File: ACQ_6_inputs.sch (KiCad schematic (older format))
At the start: 0 parts

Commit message: Layout done for ADC + LVDS and DAC -> FPGA
Signed-off-by: Alexis Jeandet <alexis.jeandet@member.fsf.org>
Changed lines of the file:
@@
 $EndDescr
 $Sheet
-S 3275 800  1450 1350
+S 3250 2550 1450 1350
 U 5F3E1AE5
 F0 "Sheet5F3E1AE4" 50
 F1 "ADC_circuit.sch" 50
-F2 "IN+" I L 3275 1225 50
-F3 "IN-" I L 3275 1350 50
+F2 "IN+" I L 3250 2975 50
+F3 "IN-" I L 3250 3100 50
+F4 "V+" I R 4700 2700 50
+F5 "V-" I R 4700 2600 50
+F6 "VDDL" I R 4700 2900 50
+F7 "OVDD" I R 4700 3000 50
+F8 "CNV" I R 4700 3350 50
+F9 "CLK" I R 4700 3450 50
+F10 "DA" I R 4700 3650 50
+F11 "DCO" I R 4700 3550 50
+F12 "VDD" I R 4700 2800 50
 $EndSheet
 Text HLabel 2975 1225 0    50   Input ~ 0
@@
 Wire Wire Line
 	2975 1350 3275 1350
-$Sheet
-S 3250 2550 1450 1350
-U 5F766F53
-F0 "sheet5F766F53" 50
-F1 "ADC_circuit.sch" 50
-F2 "IN+" I L 3250 2975 50
-F3 "IN-" I L 3250 3100 50
-$EndSheet
 Text HLabel 2950 2975 0    50   Input ~ 0
 CH2_IN+
@@
 	2950 3100 3250 3100
 $Sheet
-S 3250 4250 1450 1350
+S 6600 950  1450 1350
 U 5F7670FC
 F0 "sheet5F7670FC" 50
 F1 "ADC_circuit.sch" 50
-F2 "IN+" I L 3250 4675 50
-F3 "IN-" I L 3250 4800 50
+F2 "IN+" I L 6600 1375 50
+F3 "IN-" I L 6600 1500 50
+F4 "V+" I R 8050 1050 50
+F5 "V-" I R 8050 1175 50
+F6 "VDDL" I R 8050 1300 50
+F7 "OVDD" I R 8050 1425 50
+F8 "CNV" I R 8050 1850 50
+F9 "CLK" I R 8050 1950 50
+F10 "DA" I R 8050 2150 50
+F11 "DCO" I R 8050 2050 50
+F12 "VDD" I R 8050 1550 50
 $EndSheet
 Text HLabel 2950 4675 0    50   Input ~ 0
@@
 Wire Wire Line
 	2950 4800 3250 4800
-$Sheet
-S 6600 950  1450 1350
-U 5F7672A2
-F0 "sheet5F7672A2" 50
-F1 "ADC_circuit.sch" 50
-F2 "IN+" I L 6600 1375 50
-F3 "IN-" I L 6600 1500 50
-$EndSheet
 Text HLabel 6300 1375 0    50   Input ~ 0
 CH4_IN+
@@
 F2 "IN+" I L 6600 2975 50
 F3 "IN-" I L 6600 3100 50
+F4 "V+" I R 8050 2675 50
+F5 "V-" I R 8050 2750 50
+F6 "VDDL" I R 8050 2850 50
+F7 "OVDD" I R 8050 2925 50
+F8 "CNV" I R 8050 3475 50
+F9 "CLK" I R 8050 3575 50
+F10 "DA" I R 8050 3775 50
+F11 "DCO" I R 8050 3675 50
+F12 "VDD" I R 8050 3050 50
 $EndSheet
 Text HLabel 6300 2975 0    50   Input ~ 0
@@
 Wire Wire Line
 	6300 3100 6600 3100
-$Sheet
-S 6575 4200 1450 1350
+Text HLabel 6275 4600 0    50   Input ~ 0
+CH6_IN+
+Text HLabel 6275 4725 0    50   Input ~ 0
+CH6_IN-
+Wire Wire Line
+	6275 4600 6575 4600
+Wire Wire Line
+	6275 4725 6575 4725
+$Sheet
+S 6575 4175 1450 1350
+U 5F766F53
+F0 "sheet5F766F53" 50
+F1 "ADC_circuit.sch" 50
+F2 "IN+" I L 6575 4600 50
+F3 "IN-" I L 6575 4725 50
+F4 "V+" I R 8025 4250 50
+F5 "V-" I R 8025 4350 50
+F6 "VDDL" I R 8025 4550 50
+F7 "OVDD" I R 8025 4650 50
+F8 "CNV" I R 8025 5025 50
+F9 "CLK" I R 8025 5125 50
+F10 "DA" I R 8025 5325 50
+F11 "DCO" I R 8025 5225 50
+F12 "VDD" I R 8025 4450 50
+$EndSheet
+$Sheet
+S 3250 4250 1450 1350
 U 5F76778E
 F0 "sheet5F76778E" 50
 F1 "ADC_circuit.sch" 50
-F2 "IN+" I L 6575 4625 50
-F3 "IN-" I L 6575 4750 50
-$EndSheet
-Text HLabel 6275 4625 0    50   Input ~ 0
-CH6_IN+
-Text HLabel 6275 4750 0    50   Input ~ 0
-CH6_IN-
-Wire Wire Line
-	6275 4625 6575 4625
-Wire Wire Line
-	6275 4750 6575 4750
+F2 "IN+" I L 3250 4675 50
+F3 "IN-" I L 3250 4800 50
+F4 "V+" I R 4700 4325 50
+F5 "V-" I R 4700 4425 50
+F6 "VDDL" I R 4700 4525 50
+F7 "OVDD" I R 4700 4625 50
+F8 "CNV" I R 4700 5125 50
+F9 "CLK" I R 4700 5225 50
+F10 "DA" I R 4700 5425 50
+F11 "DCO" I R 4700 5325 50
+F12 "VDD" I R 4700 4725 50
+$EndSheet
+Text HLabel 4925 1700 2    50   Input ~ 0
+ADC1_CNV
+Text HLabel 4925 1800 2    50   Input ~ 0
+ADC1_CLK
+Text HLabel 4925 1900 2    50   Input ~ 0
+ADC1_DCO
+Text HLabel 4925 2000 2    50   Input ~ 0
+ADC1_DA
+Wire Wire Line
+	4725 1700 4925 1700
+Wire Wire Line
+	4725 1800 4925 1800
+Wire Wire Line
+	4725 1900 4925 1900
+Wire Wire Line
+	4725 2000 4925 2000
+Text HLabel 8250 1850 2    50   Input ~ 0
+ADC4_CNV
+Text HLabel 8250 1950 2    50   Input ~ 0
+ADC4_CLK
+Text HLabel 8250 2050 2    50   Input ~ 0
+ADC4_DCO
+Text HLabel 8250 2150 2    50   Input ~ 0
+ADC4_DA
+Wire Wire Line
+	8050 1850 8250 1850
+Wire Wire Line
+	8050 1950 8250 1950
+Wire Wire Line
+	8050 2050 8250 2050
+Wire Wire Line
+	8050 2150 8250 2150
+Text HLabel 8250 3475 2    50   Input ~ 0
+ADC5_CNV
+Text HLabel 8250 3575 2    50   Input ~ 0
+ADC5_CLK
+Text HLabel 8250 3675 2    50   Input ~ 0
+ADC5_DCO
+Text HLabel 8250 3775 2    50   Input ~ 0
+ADC5_DA
+Wire Wire Line
+	8050 3475 8250 3475
+Wire Wire Line
+	8050 3575 8250 3575
+Wire Wire Line
+	8050 3675 8250 3675
+Wire Wire Line
+	8050 3775 8250 3775
+Text HLabel 8225 5025 2    50   Input ~ 0
+ADC6_CNV
+Text HLabel 8225 5125 2    50   Input ~ 0
+ADC6_CLK
+Text HLabel 8225 5225 2    50   Input ~ 0
+ADC6_DCO
+Text HLabel 8225 5325 2    50   Input ~ 0
+ADC6_DA
+Wire Wire Line
+	8025 5025 8225 5025
+Wire Wire Line
+	8025 5125 8225 5125
+Wire Wire Line
+	8025 5225 8225 5225
+Wire Wire Line
+	8025 5325 8225 5325
+Text HLabel 4900 5125 2    50   Input ~ 0
+ADC3_CNV
+Text HLabel 4900 5225 2    50   Input ~ 0
+ADC3_CLK
+Text HLabel 4900 5325 2    50   Input ~ 0
+ADC3_DCO
+Text HLabel 4900 5425 2    50   Input ~ 0
+ADC3_DA
+Wire Wire Line
+	4700 5125 4900 5125
+Wire Wire Line
+	4700 5225 4900 5225
+Wire Wire Line
+	4700 5325 4900 5325
+Wire Wire Line
+	4700 5425 4900 5425
+Text HLabel 4900 3350 2    50   Input ~ 0
+ADC2_CNV
+Text HLabel 4900 3450 2    50   Input ~ 0
+ADC2_CLK
+Text HLabel 4900 3550 2    50   Input ~ 0
+ADC2_DCO
+Text HLabel 4900 3650 2    50   Input ~ 0
+ADC2_DA
+Wire Wire Line
+	4700 3350 4900 3350
+Wire Wire Line
+	4700 3450 4900 3450
+Wire Wire Line
+	4700 3550 4900 3550
+Wire Wire Line
+	4700 3650 4900 3650
+$Sheet
+S 3275 800  1450 1350
+U 5F7672A2
+F0 "sheet5F7672A2" 50
+F1 "ADC_circuit.sch" 50
+F2 "IN+" I L 3275 1225 50
+F3 "IN-" I L 3275 1350 50
+F4 "V+" I R 4725 875 50
+F5 "V-" I R 4725 975 50
+F6 "VDDL" I R 4725 1100 50
+F7 "OVDD" I R 4725 1200 50
+F8 "CNV" I R 4725 1700 50
+F9 "CLK" I R 4725 1800 50
+F10 "DA" I R 4725 2000 50
+F11 "DCO" I R 4725 1900 50
+F12 "VDD" I R 4725 1325 50
+$EndSheet
 $EndSCHEMATC

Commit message: Layout complete, needs silk screen cleanup and few checks
Signed-off-by: Alexis Jeandet <alexis.jeandet@member.fsf.org>
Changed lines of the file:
@@
 F2 "IN+" I L 3250 2975 50
 F3 "IN-" I L 3250 3100 50
-F4 "V+" I R 4700 2700 50
-F5 "V-" I R 4700 2600 50
+F4 "V+" I R 4700 2600 50
+F5 "V-" I R 4700 2700 50
 F6 "VDDL" I R 4700 2900 50
 F7 "OVDD" I R 4700 3000 50
@@
 F5 "V-" I R 4700 4425 50
 F6 "VDDL" I R 4700 4525 50
-F7 "OVDD" I R 4700 4625 50
+F7 "OVDD" I R 4700 4725 50
 F8 "CNV" I R 4700 5125 50
 F9 "CLK" I R 4700 5225 50
 F10 "DA" I R 4700 5425 50
 F11 "DCO" I R 4700 5325 50
-F12 "VDD" I R 4700 4725 50
+F12 "VDD" I R 4700 4625 50
 $EndSheet
 Text HLabel 4925 1700 2    50   Input ~ 0
@@
 F12 "VDD" I R 4725 1325 50
 $EndSheet
+Text HLabel 975  700  0    50   BiDi ~ 0
+5V
+Text HLabel 975  800  0    50   BiDi ~ 0
+-5V
+Text HLabel 975  900  0    50   BiDi ~ 0
+2.5V
+Text HLabel 975  1000 0    50   BiDi ~ 0
+#2.5V
+Wire Wire Line
+	975  700  1200 700
+Wire Wire Line
+	975  800  1200 800
+Wire Wire Line
+	975  900  1200 900
+Wire Wire Line
+	975  1000 1200 1000
+Text Label 1200 700  0    50   ~ 0
+5V
+Text Label 1200 800  0    50   ~ 0
+-5V
+Text Label 1200 900  0    50   ~ 0
+2.5V
+Text Label 1200 1000 0    50   ~ 0
+#2.5V
+Text Label 4900 875  0    50   ~ 0
+5V
+Text Label 4900 975  0    50   ~ 0
+-5V
+Text Label 4900 1100 0    50   ~ 0
+2.5V
+Text Label 4900 1200 0    50   ~ 0
+#2.5V
+Wire Wire Line
+	4725 875  4900 875
+Wire Wire Line
+	4725 975  4900 975
+Wire Wire Line
+	4725 1100 4900 1100
+Wire Wire Line
+	4725 1200 4900 1200
+Wire Wire Line
+	4725 1325 4900 1325
+Text Label 4900 1325 0    50   ~ 0
+5V
+Text Label 4875 2600 0    50   ~ 0
+5V
+Text Label 4875 2700 0    50   ~ 0
+-5V
+Text Label 4875 2900 0    50   ~ 0
+2.5V
+Text Label 4875 3000 0    50   ~ 0
+#2.5V
+Wire Wire Line
+	4700 2600 4875 2600
+Wire Wire Line
+	4700 2700 4875 2700
+Wire Wire Line
+	4700 2900 4875 2900
+Wire Wire Line
+	4700 3000 4875 3000
+Wire Wire Line
+	4700 2800 4875 2800
+Text Label 4875 2800 0    50   ~ 0
+5V
+Text Label 4875 4325 0    50   ~ 0
+5V
+Text Label 4875 4425 0    50   ~ 0
+-5V
+Text Label 4875 4625 0    50   ~ 0
+2.5V
+Text Label 4875 4725 0    50   ~ 0
+#2.5V
+Wire Wire Line
+	4700 4325 4875 4325
+Wire Wire Line
+	4700 4425 4875 4425
+Wire Wire Line
+	4700 4625 4875 4625
+Wire Wire Line
+	4700 4725 4875 4725
+Wire Wire Line
+	4700 4525 4875 4525
+Text Label 4875 4525 0    50   ~ 0
+5V
+Text Label 8225 1050 0    50   ~ 0
+5V
+Text Label 8225 1175 0    50   ~ 0
+-5V
+Text Label 8225 1300 0    50   ~ 0
+2.5V
+Text Label 8225 1425 0    50   ~ 0
+#2.5V
+Wire Wire Line
+	8050 1050 8225 1050
+Wire Wire Line
+	8050 1175 8225 1175
+Wire Wire Line
+	8050 1300 8225 1300
+Wire Wire Line
+	8050 1425 8225 1425
+Wire Wire Line
+	8050 1550 8225 1550
+Text Label 8225 1550 0    50   ~ 0
+5V
+Text Label 8225 2675 0    50   ~ 0
+5V
+Text Label 8225 2750 0    50   ~ 0
+-5V
+Text Label 8225 2850 0    50   ~ 0
+2.5V
+Text Label 8225 2925 0    50   ~ 0
+#2.5V
+Wire Wire Line
+	8050 2675 8225 2675
+Wire Wire Line
+	8050 2750 8225 2750
+Wire Wire Line
+	8050 2850 8225 2850
+Wire Wire Line
+	8050 2925 8225 2925
+Wire Wire Line
+	8050 3050 8225 3050
+Text Label 8225 3050 0    50   ~ 0
+5V
+Text Label 8200 4250 0    50   ~ 0
+5V
+Text Label 8200 4350 0    50   ~ 0
+-5V
+Text Label 8200 4550 0    50   ~ 0
+2.5V
+Text Label 8200 4650 0    50   ~ 0
+#2.5V
+Wire Wire Line
+	8025 4250 8200 4250
+Wire Wire Line
+	8025 4350 8200 4350
+Wire Wire Line
+	8025 4550 8200 4550
+Wire Wire Line
+	8025 4650 8200 4650
+Wire Wire Line
+	8025 4450 8200 4450
+Text Label 8200 4450 0    50   ~ 0
+5V
 $EndSCHEMATC

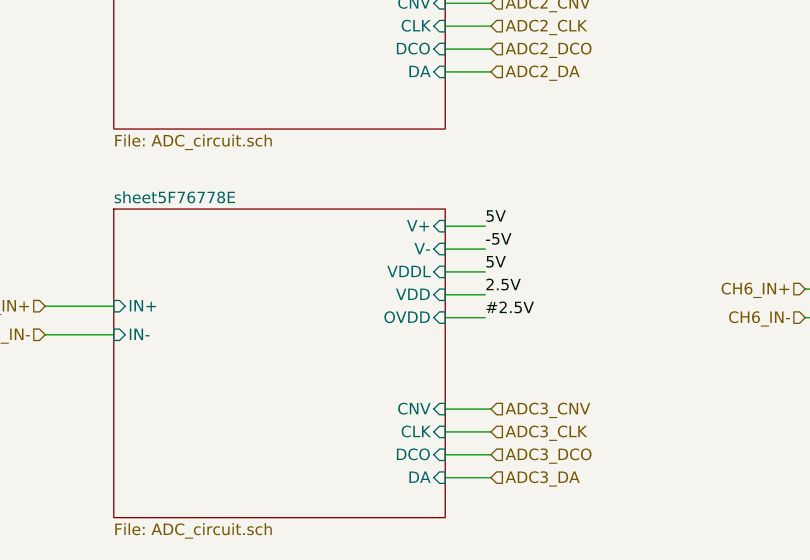
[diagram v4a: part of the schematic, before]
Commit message: Fixed mistake on one ADC chan power line
Signed-off-by: Alexis Jeandet <alexis.jeandet@member.fsf.org>
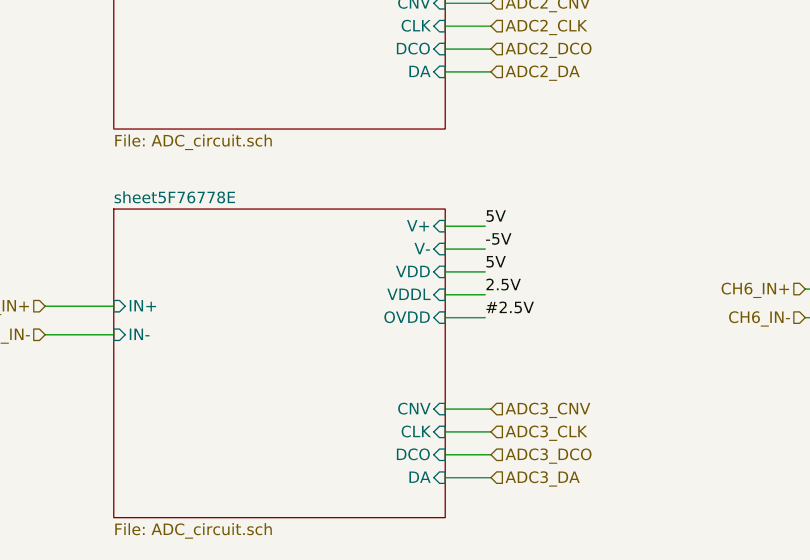
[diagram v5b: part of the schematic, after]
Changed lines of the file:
@@
 F4 "V+" I R 4700 4325 50
 F5 "V-" I R 4700 4425 50
-F6 "VDDL" I R 4700 4525 50
+F6 "VDDL" I R 4700 4625 50
 F7 "OVDD" I R 4700 4725 50
 F8 "CNV" I R 4700 5125 50
@@
 F10 "DA" I R 4700 5425 50
 F11 "DCO" I R 4700 5325 50
-F12 "VDD" I R 4700 4625 50
+F12 "VDD" I R 4700 4525 50
 $EndSheet
 Text HLabel 4925 1700 2    50   Input ~ 0
